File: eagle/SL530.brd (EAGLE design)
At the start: 100 x 100 mm, 42 parts, among them IC4 74LVC1G17DBV, IC5 74LVC1G17DBV, U1 LM1117, X1 MC68000

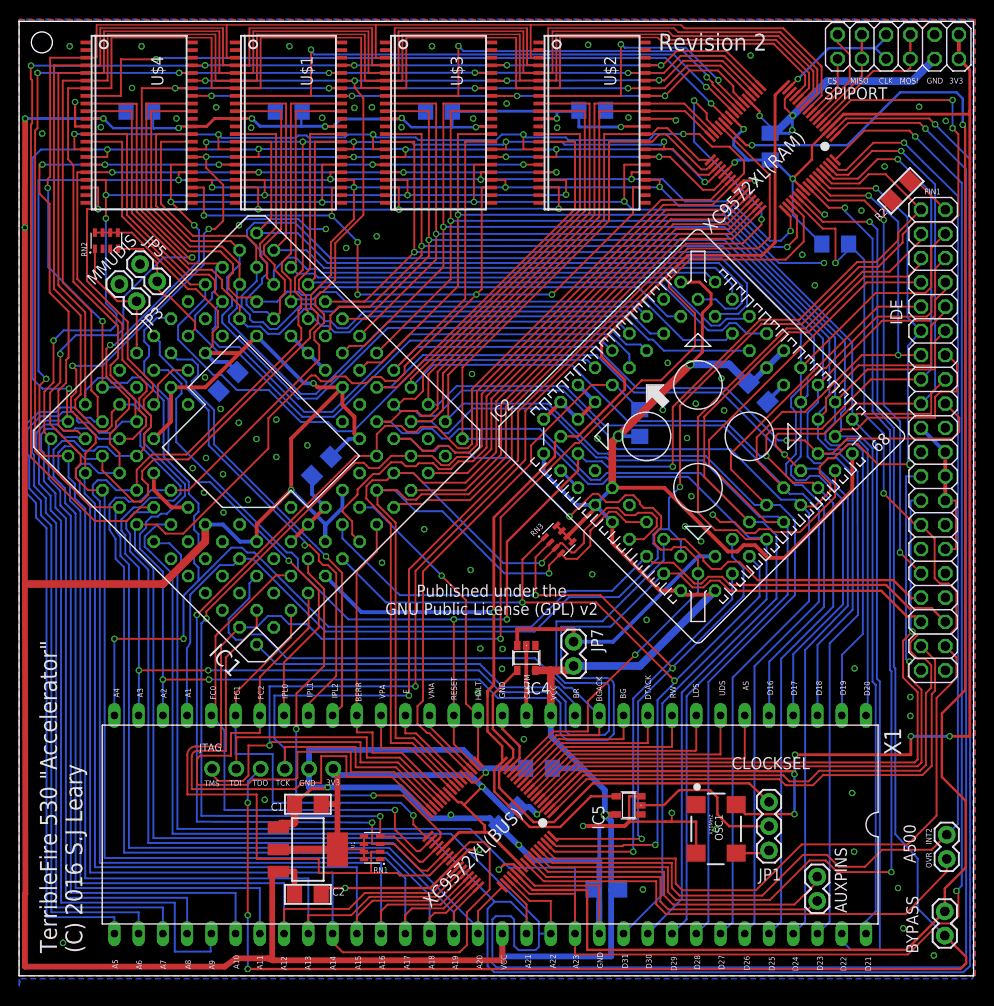
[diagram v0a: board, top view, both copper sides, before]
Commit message: Modifications to the TF530. upgrade to eagle 8. Added IPL lines to the bus CPLD. Significant re-routing of the Bus CPLD traces. Incremented version to revision 3 Beefed up power rails. improved routing over the bus cpld. better ground planes.
No CPLD updates yet.. to follow.
Added 2 more decoupling caps for the 030
Removed unused DSACK1/A14/AUX0/AUX1

I have left in OVR and INT2 for test purposes.
These shouldn't need connected.

removed the test traces for A14
removed A7 from the RAM cpld and created a single header pin. potentially for SPI Interrupts (Active HIGH).

Verified pass the DRC checks.
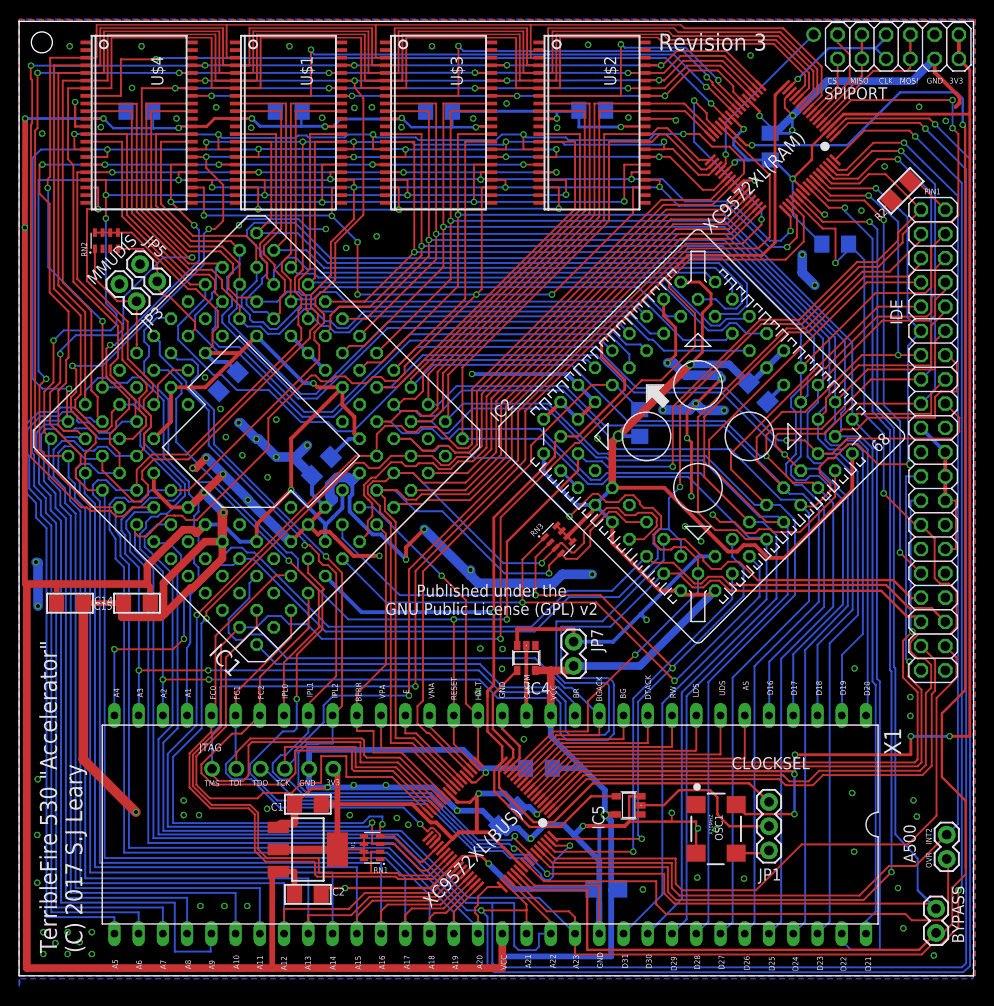
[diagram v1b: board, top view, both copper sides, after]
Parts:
- removed AUXPINS: AUXPINS, SparkFun-Retired:1X02
- added C14, C15: 10uF, microbuilder:1206
- moved BYPASS 2.44 mm to (96.1, 4.50), turned to 90 degrees
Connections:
- removed net AUX0: AUXPINS.1, XC9572XL(BUS).58
- removed net AUX1: AUXPINS.2, XC9572XL(BUS).57
- new net SPARE: XC9572XL(RAM).36
- net A14: no longer XC9572XL(BUS).40
- net A7: no longer XC9572XL(RAM).36
- net AVEC: now also XC9572XL(BUS).63; no longer XC9572XL(BUS).35
- net DSACK0: no longer XC9572XL(BUS).63
- net FC0: now also XC9572XL(BUS).40; no longer XC9572XL(BUS).34
- net FC1: now also XC9572XL(BUS).35; no longer XC9572XL(BUS).33
- net GND: now also C14.2, C15.2
- net IPL1: now also XC9572XL(BUS).57
- net IPL2: now also XC9572XL(BUS).58
- net VCC: now also C14.1, C15.1
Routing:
- net GND: track 315.8 -> 540.2 mm, vias 93 -> 125
- net A14: track 243.7 -> 188.2 mm, vias 7 -> 6
- net IPL2: track 47.2 -> 86.0 mm, vias 1 -> 2
- net IPL1: track 49.5 -> 87.9 mm, vias 1 -> 2
- net AUX0: track 34.9 -> 0.00 mm
- net AUX1: track 34.2 -> 0.00 mm
- net DSACK0: track 94.7 -> 65.5 mm, vias 3 -> 2
- net AVEC: track 44.8 -> 70.1 mm
- net TDO: track 187.4 -> 162.1 mm, vias 4 -> 2
- net A7: track 186.5 -> 167.4 mm, vias 6 -> 5
- net SPARE: track 0.00 -> 18.2 mm, vias 0 -> 2
- net FC0: track 54.7 -> 62.8 mm, vias 1 -> 0
- net TMS: track 134.1 -> 141.9 mm, vias 2 -> 1
- net VCC: track 561.0 -> 566.8 mm
- net SIZ0: track 129.1 -> 134.6 mm
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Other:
- board text added: "Revision 3"
- board text added: "TerribleFire 530 "Accelerator" (C) 2017 S.J Leary"
- board text removed: "Revision 2"
- board text removed: "TerribleFire 530 "Accelerator" (C) 2016 S.J Leary"

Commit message: Bit of a clean up of the silkscreen Really beefed up VCC to the CPU more ground beefing added an experimental (optional) resistor to load the CPU clock line. added 2 more 0603 caps. One for the CPU and one for the FPU. This version was submitted to dirtypcsb as revision 3
Bit more tidy up on the routing around the bus cpld.
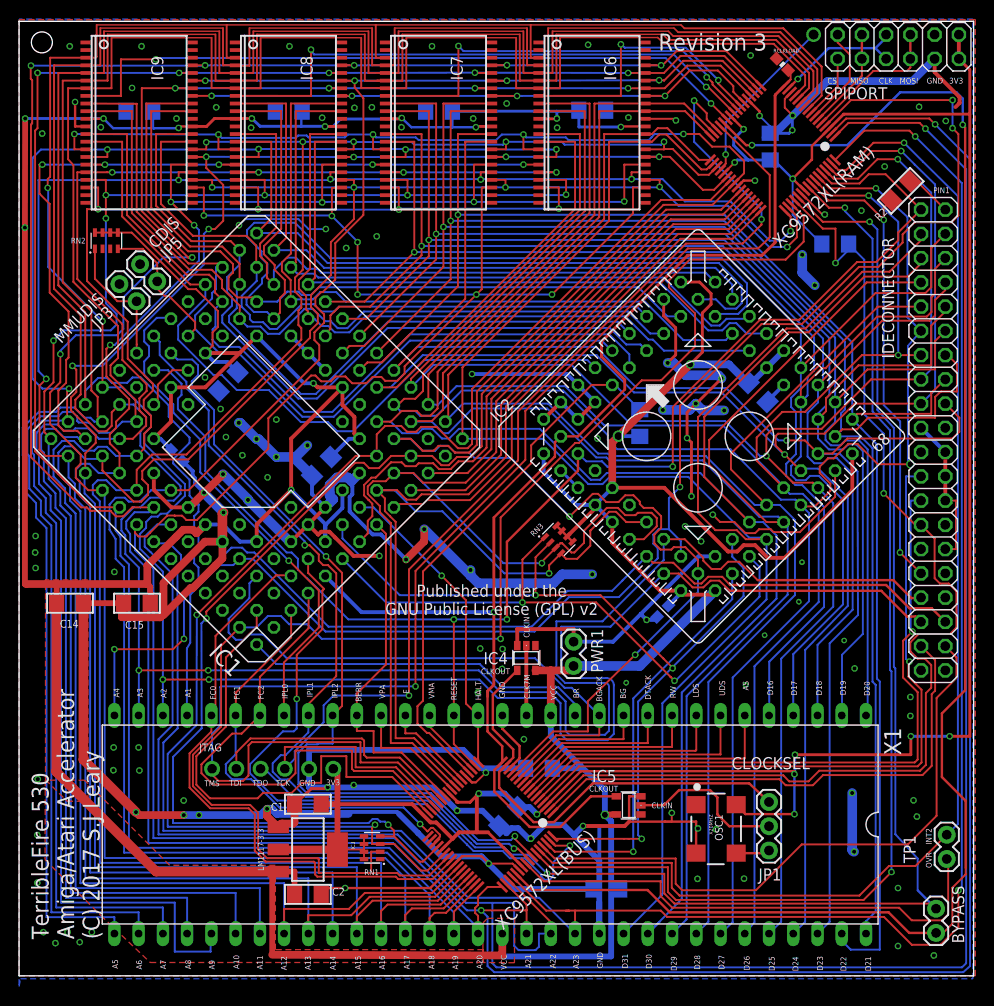
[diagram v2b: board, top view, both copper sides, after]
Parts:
- added C16, C17: 0.1uF, SparkFun-Capacitors:0603-CAP
- added RCLKLOAD: INF, SparkFun-Resistors:0603
- IC3: value LM1117 -> LM1117-3.3
- R3: value 10K -> 47K
- TP1: value A500 -> TP1
- renumbered A500 to TP1, IDE to IDECONNECTOR, JP7 to PWR1, U$1 to IC8, U$2 to IC6, U$3 to IC7, U$4 to IC9, U1 to IC3
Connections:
- net CLKCPU: now also RCLKLOAD.1
- net GND: now also C16.2, C17.2, RCLKLOAD.2
- net VCC: now also C16.1, C17.1
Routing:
- net GND: track 540.2 -> 574.7 mm, vias 125 -> 124
- net VCC: track 566.8 -> 548.4 mm
- net TDINT: track 171.9 -> 166.8 mm
- net CLKCPU: track 130.3 -> 132.3 mm
- net A4: track 294.9 -> 296.4 mm
- net IPL0: track 54.1 -> 53.3 mm
- net OVR: track 54.3 -> 53.8 mm
- added copper zone on layer 1, net VCC
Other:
- board text added: "CLKIN"
- board text added: "CLKOUT"
- board text added: "TerribleFire 530 Amiga/Atari Accelerator (C) 2017 S.J Leary"
- board text removed: "TerribleFire 530 "Accelerator" (C) 2017 S.J Leary"
